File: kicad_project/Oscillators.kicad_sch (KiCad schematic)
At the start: 8 parts, among them X1 12.000MHz

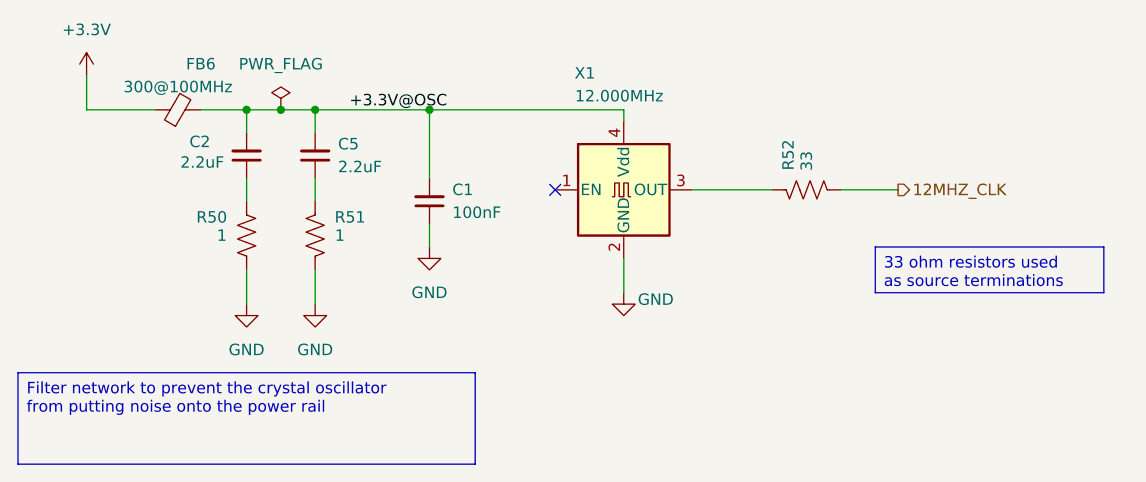
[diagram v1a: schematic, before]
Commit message: Finish schematic and placement for all remaining RP2354 power passives
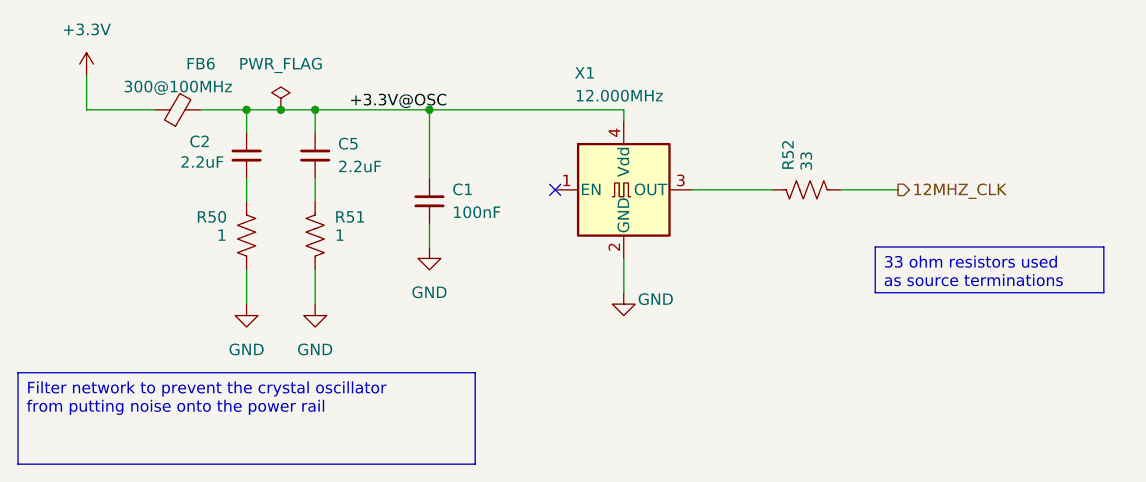
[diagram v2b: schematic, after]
